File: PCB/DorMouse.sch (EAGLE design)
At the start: 56 parts, among them IC1 LM340MP-05, IC2 MAX1551, U1 STM32F10XRXT6, X1 MINI-USB-UX60-MB-5ST

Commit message: Silkscreen work: values and mice
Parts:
- BAROMETER: device Swallow:MPL115A1 -> DorMouse:MPL115A1
- HIGH-G_ACC: device Swallow:ADXL377 -> DorMouse:ADXL377
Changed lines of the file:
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@@
 <part name="P+6" library="supply1" deviceset="VCC" device=""/>
 <part name="SUPPLY8" library="supply2" deviceset="GND" device=""/>
-<part name="BAROMETER" library="Swallow" deviceset="MPL115A1" device=""/>
+<part name="BAROMETER" library="DorMouse" deviceset="MPL115A1" device=""/>
 <part name="P+7" library="supply1" deviceset="VCC" device=""/>
 <part name="SUPPLY9" library="supply2" deviceset="GND" device=""/>
@@
 <part name="SUPPLY4" library="supply2" deviceset="GND" device=""/>
 <part name="SUPPLY12" library="supply2" deviceset="GND" device=""/>
-<part name="HIGH-G_ACC" library="Swallow" deviceset="ADXL377" device=""/>
+<part name="HIGH-G_ACC" library="DorMouse" deviceset="ADXL377" device=""/>
 <part name="P+10" library="supply1" deviceset="VCC" device=""/>
 <part name="SUPPLY18" library="supply2" deviceset="GND" device=""/>

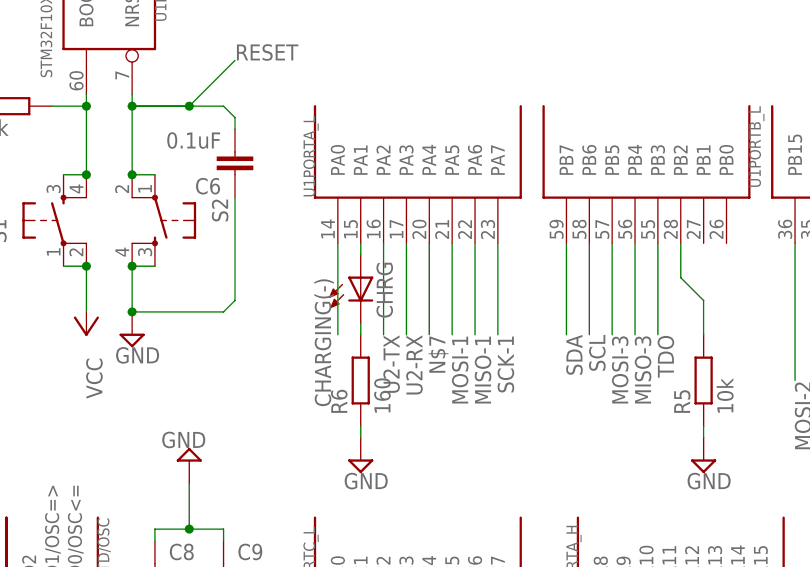
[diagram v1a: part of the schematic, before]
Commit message: Add labels for GPS
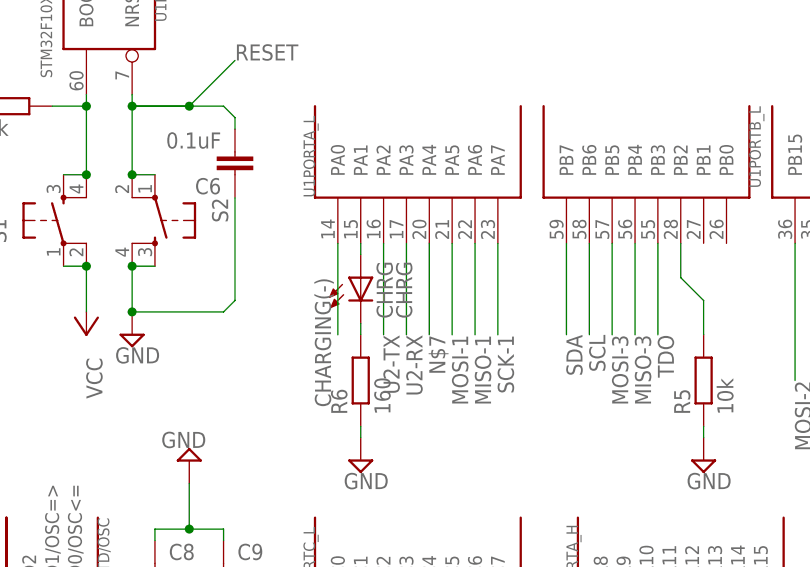
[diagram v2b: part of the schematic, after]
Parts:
- CHRG: value (none) -> CHRG
- GENERAL: value RED-GREEN_LED -> Status
- GPS-LED: value RED-GREEN_LED -> GPS
- SD-LED: value RED-GREEN_LED -> SD-C
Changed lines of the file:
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@@
 <part name="S1" library="SparkFun" deviceset="TAC_SWITCH" device="SMD"/>
 <part name="S2" library="SparkFun" deviceset="TAC_SWITCH" device="SMD"/>
-<part name="GPS-LED" library="DorMouse" deviceset="RED-GREEN_LED" device=""/>
-<part name="SD-LED" library="DorMouse" deviceset="RED-GREEN_LED" device=""/>
-<part name="GENERAL" library="DorMouse" deviceset="RED-GREEN_LED" device=""/>
+<part name="GPS-LED" library="DorMouse" deviceset="RED-GREEN_LED" device="" value="GPS"/>
+<part name="SD-LED" library="DorMouse" deviceset="RED-GREEN_LED" device="" value="SD-C"/>
+<part name="GENERAL" library="DorMouse" deviceset="RED-GREEN_LED" device="" value="Status"/>
 <part name="SUPPLY30" library="supply2" deviceset="GND" device=""/>
 <part name="SUPPLY31" library="supply2" deviceset="GND" device=""/>
@@
 <part name="C12" library="rcl" deviceset="C-EU" device="C0402" value="0.01uF"/>
 <part name="SUPPLY37" library="supply2" deviceset="GND" device=""/>
-<part name="CHRG" library="led" deviceset="LED" device="CHIPLED_0603"/>
+<part name="CHRG" library="led" deviceset="LED" device="CHIPLED_0603" value="CHRG"/>
 <part name="R6" library="rcl" deviceset="R-EU_" device="R0402" value="160"/>
 <part name="SUPPLY38" library="supply2" deviceset="GND" device=""/>

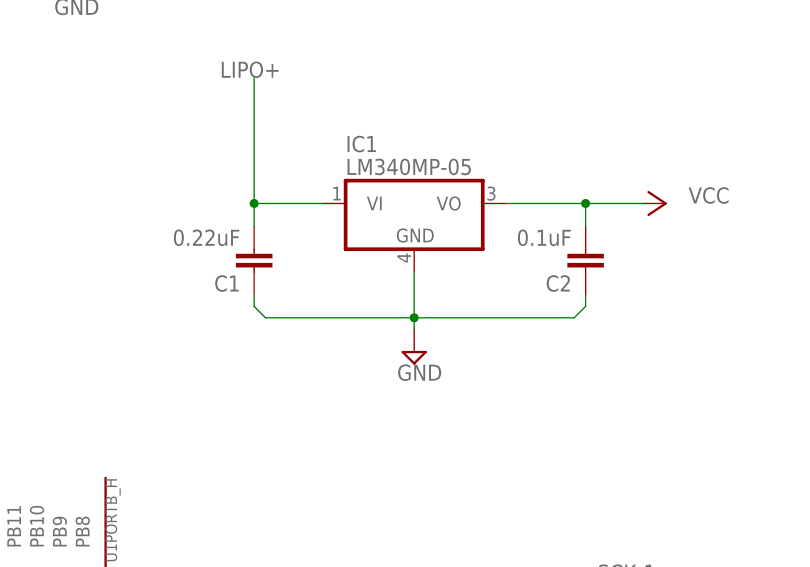
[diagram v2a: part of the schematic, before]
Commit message: Connect pad 2 of LDO reg to GND
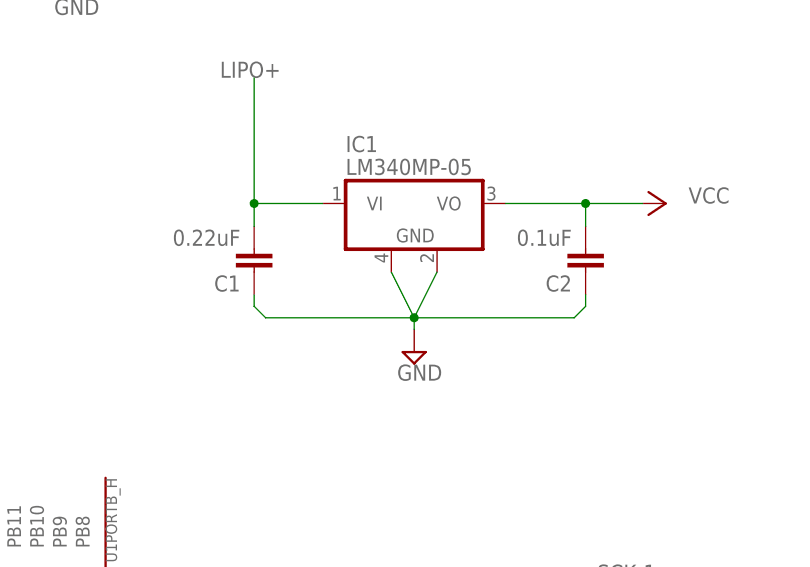
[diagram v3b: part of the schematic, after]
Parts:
- IC1: device linear:LM340MP-05 -> DorMouse:LM340MP-05
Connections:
- net GND: now also IC1.GND1
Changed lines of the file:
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@@
 <part name="P+1" library="supply1" deviceset="VCC" device=""/>
 <part name="SUPPLY1" library="supply2" deviceset="GND" device=""/>
-<part name="IC1" library="linear" deviceset="LM340?-*" device="MP" technology="05"/>
+<part name="IC1" library="DorMouse" deviceset="LM340?-*" device="MP" technology="05"/>
 <part name="C1" library="rcl" deviceset="C-EU" device="C0402" value="0.22uF"/>
 <part name="C2" library="rcl" deviceset="C-EU" device="C0402" value="0.1uF"/>
@@
 <wire x1="45.72" y1="73.66" x2="27.94" y2="73.66" width="0.1524" layer="91"/>
 <pinref part="IC1" gate="A" pin="GND"/>
-<wire x1="27.94" y1="73.66" x2="27.94" y2="78.74" width="0.1524" layer="91"/>
+<wire x1="27.94" y1="73.66" x2="25.4" y2="78.74" width="0.1524" layer="91"/>
 <junction x="27.94" y="73.66"/>
-</segment>
-<segment>
+<pinref part="IC1" gate="A" pin="GND1"/>
+<wire x1="30.48" y1="78.74" x2="27.94" y2="73.66" width="0.1524" layer="91"/>
+</segment>
+<segment>
